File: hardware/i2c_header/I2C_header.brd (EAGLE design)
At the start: 27 x 30.5 mm, 6 parts, among them X6 I2C

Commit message: Board dimension added
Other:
- board size 27 x 30.5 mm -> 27 x 30.7 mm
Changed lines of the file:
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@@
 <setting verticaltext="up"/>
 </settings>
-<grid distance="0.1" unitdist="mm" unit="mm" style="lines" multiple="1" display="yes" altdistance="0.000123031496" altunitdist="mil" altunit="mil"/>
+<grid distance="10" unitdist="mm" unit="mm" style="lines" multiple="1" display="yes" altdistance="0.000123031496" altunitdist="mil" altunit="mil"/>
 <layers>
 <layer number="1" name="Top" color="4" fill="1" visible="yes" active="yes"/>
@@
 <hole x="20" y="20" drill="2.2"/>
 <circle x="20" y="20" radius="2" width="0" layer="41"/>
+<wire x1="1.9739625" y1="-0.792025" x2="-0.0260375" y2="1.207975" width="0" layer="20" curve="-90"/>
+<wire x1="-0.0260375" y1="1.207975" x2="-0.0260375" y2="8.707975" width="0" layer="20"/>
+<wire x1="-0.0260375" y1="8.707975" x2="-0.5260375" y2="9.207975" width="0" layer="20" curve="90"/>
+<wire x1="-0.5260375" y1="9.207975" x2="-1.0260375" y2="9.207975" width="0" layer="20"/>
+<wire x1="-1.0260375" y1="9.207975" x2="-3.5260375" y2="11.707975" width="0" layer="20" curve="-90"/>
+<wire x1="-3.5260375" y1="11.707975" x2="-3.5260375" y2="21.707975" width="0" layer="20"/>
+<wire x1="-3.5260375" y1="21.707975" x2="-0.0260375" y2="24.207975" width="0" layer="20" curve="-90"/>
+<wire x1="-0.0260375" y1="24.207975" x2="0.9739625" y2="24.207975" width="0" layer="20"/>
+<wire x1="0.9739625" y1="24.207975" x2="1.4739625" y2="24.707975" width="0" layer="20" curve="90"/>
+<wire x1="1.4739625" y1="24.707975" x2="1.4739625" y2="28.207975" width="0" layer="20"/>
+<wire x1="1.4739625" y1="28.207975" x2="2.4739625" y2="29.707975" width="0" layer="20" curve="-90"/>
+<wire x1="17.9739625" y1="-0.792025" x2="19.9739625" y2="1.207975" width="0" layer="20" curve="90"/>
+<wire x1="19.9739625" y1="1.207975" x2="19.9739625" y2="8.707975" width="0" layer="20"/>
+<wire x1="19.9739625" y1="8.707975" x2="20.4739625" y2="9.207975" width="0" layer="20" curve="-90"/>
+<wire x1="20.4739625" y1="9.207975" x2="20.9739625" y2="9.207975" width="0" layer="20"/>
+<wire x1="20.9739625" y1="9.207975" x2="23.4739625" y2="11.707975" width="0" layer="20" curve="90"/>
+<wire x1="23.4739625" y1="11.707975" x2="23.4739625" y2="21.707975" width="0" layer="20"/>
+<wire x1="23.4739625" y1="21.707975" x2="19.9739625" y2="24.207975" width="0" layer="20" curve="90"/>
+<wire x1="19.9739625" y1="24.207975" x2="18.9739625" y2="24.207975" width="0" layer="20"/>
+<wire x1="18.9739625" y1="24.207975" x2="18.4739625" y2="24.707975" width="0" layer="20" curve="-90"/>
+<wire x1="18.4739625" y1="24.707975" x2="18.4739625" y2="28.207975" width="0" layer="20"/>
+<wire x1="18.4739625" y1="28.207975" x2="17.4739625" y2="29.707975" width="0" layer="20" curve="90"/>
+<wire x1="17.4739625" y1="29.707975" x2="2.4739625" y2="29.707975" width="0" layer="20"/>
+<wire x1="17.9739625" y1="-0.792025" x2="1.9739625" y2="-0.792025" width="0" layer="20"/>
 </plain>
 <attributes>

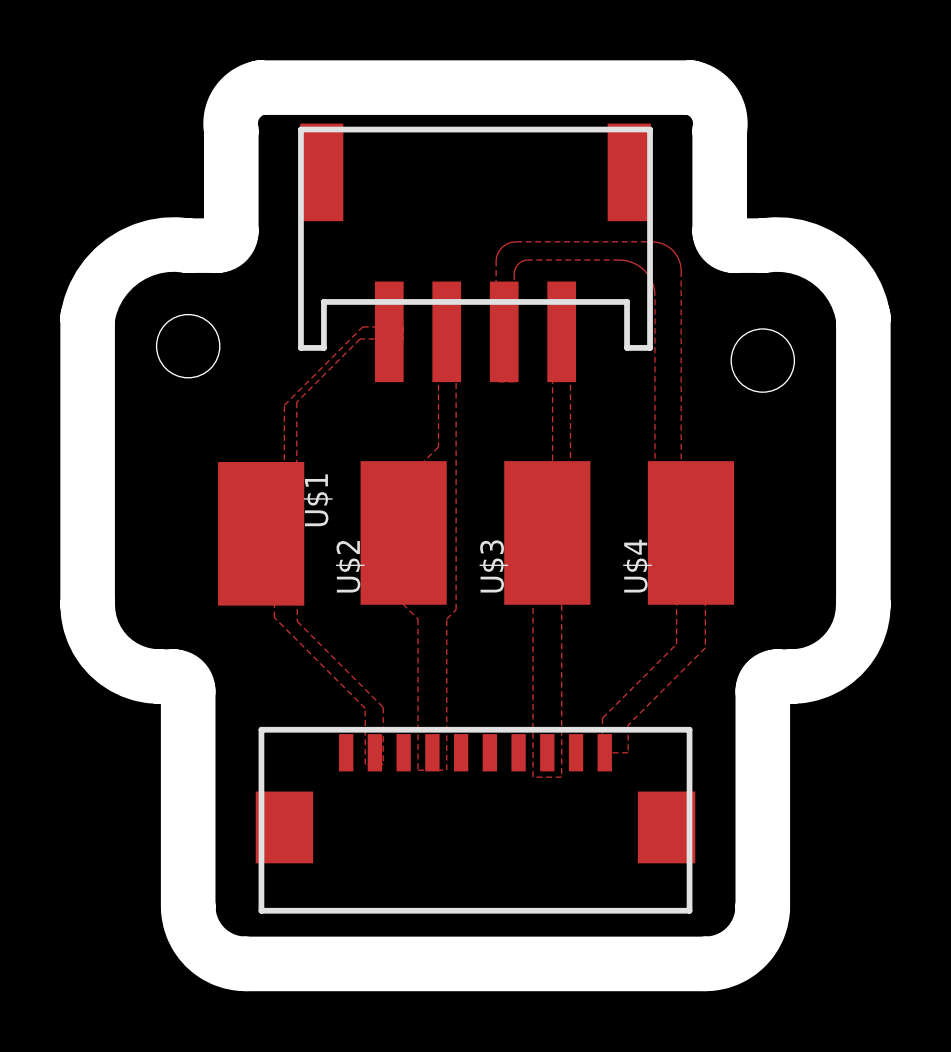
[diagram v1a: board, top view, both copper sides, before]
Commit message: header pinout changed
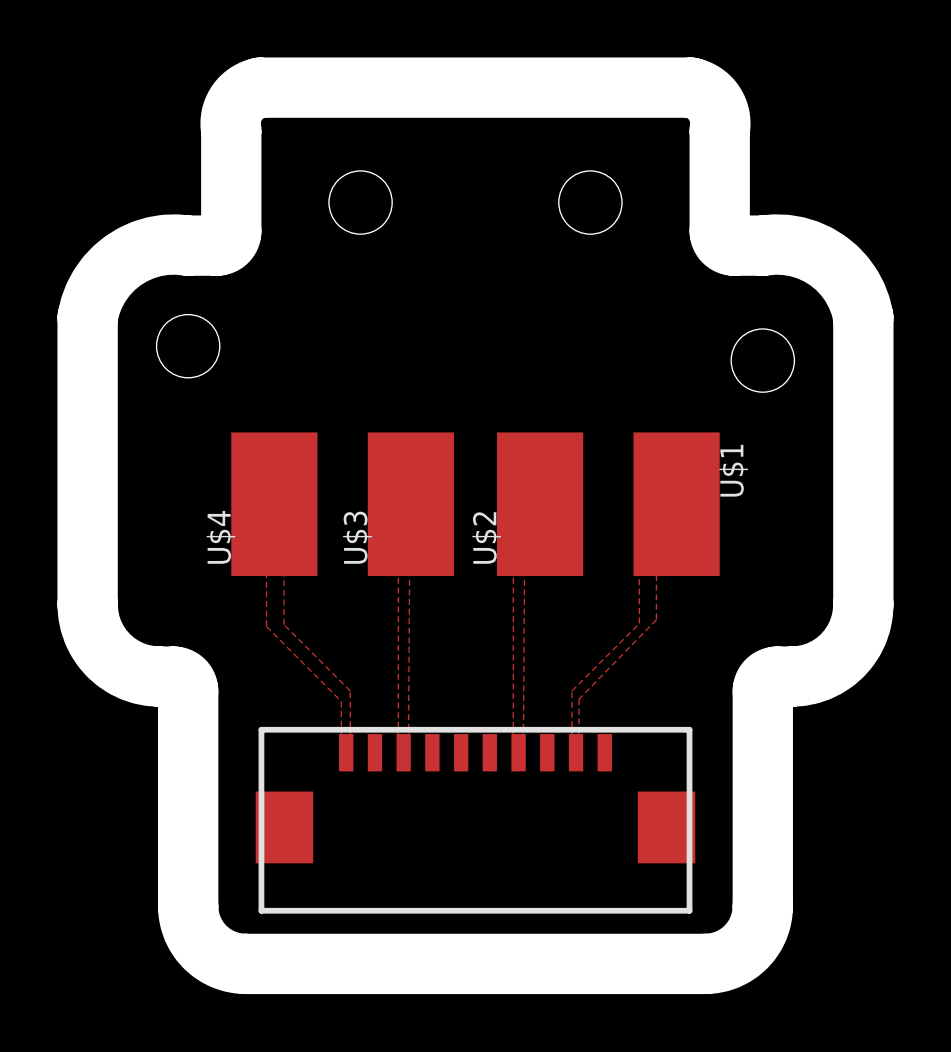
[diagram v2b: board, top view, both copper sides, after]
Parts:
- removed X6: I2C, RAK3172_board:JST-PH_4
- moved U$4 14.5 mm to (3.00, 15.0)
- moved U$1 14.5 mm to (17.0, 15.0)
- moved U$2 4.85 mm to (12.2, 15.0)
- moved U$3 4.85 mm to (7.75, 15.0)
- renumbered X1 to X2
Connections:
- removed net ALERT0: X2.P$1
- removed net ALERT1: X2.P$3
- removed net ALERT2: X2.P$5
- removed net ALERT3: X2.P$7
- removed net ALERT4: X2.P$9
- removed net N$6: X2.P$6
- net +3V3: now also X2.P$3; no longer X2.P$8, X6.1
- net GND: now also X2.P$1; no longer X2.P$10, X6.2
- net SCL: now also X2.P$9; no longer X2.P$2, X6.4
- net SDA: now also X2.P$7; no longer X2.P$4, X6.3
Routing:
- net SCL: track 1.02 -> 0.00 mm
- net +3V3: track 0.71 -> 0.00 mm

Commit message: Latest hardware designs
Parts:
- added Q1: BSS84, SIG_Parts:SOT-23-3
- added Q2: BSS138, SIG_Parts:SOT-23-3
- added R1, R2: (no value), SIG_Parts:SMD_0805
- added U$5: PAD3.0X5.0, SIG_Parts:PAD3X5
- added X1: 22-23-2021, con-molex:22-23-2021
- X2: value (none) -> 22-23-2021; device SIG_Parts:FFC_1.0X10_LARGE_PADS -> con-molex:22-23-2021
- moved U$3 3.88 mm to (4.00, 14.0)
- moved U$2 3.64 mm to (15.8, 14.0)
- moved U$1 3.16 mm to (20.0, 14.0)
- moved U$4 3.16 mm to (0.00, 14.0)
- moved X2 3.00 mm to (7.00, 5.00)
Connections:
- new net N$1: Q1.3, X2.2
- new net N$2: Q1.1, Q2.3, R1.2
- new net PWR_ON: Q2.1, R2.2, U$5.P$1
- net +3V3: now also Q1.2, R1.1; no longer X2.P$3
- net GND: now also Q2.2, R2.1, X2.1; no longer X2.P$1
- net SCL: now also X1.2; no longer X2.P$9
- net SDA: now also X1.1; no longer X2.P$7
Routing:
- net GND: track 0.00 -> 34.9 mm
- net +3V3: track 0.00 -> 14.4 mm
- net SCL: track 0.00 -> 11.0 mm
- net SDA: track 0.00 -> 10.3 mm
- net N$2: track 0.00 -> 9.19 mm
- net PWR_ON: track 0.00 -> 8.07 mm
- net N$1: track 0.00 -> 5.27 mm
- removed copper zone on layer 1, net +3V3
- removed copper zone on layer 1, net GND
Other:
- board size 27 x 30.7 mm -> 27 x 27 mm
